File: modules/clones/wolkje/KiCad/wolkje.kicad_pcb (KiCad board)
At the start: 2 copper layers, 90 x 110 mm, 137 parts, among them J1 IN_L, J10 SIZE_IN, J11 BLEND_IN, J12 TEXTURE_IN, J2 OUT_L, J3 IN_R, J4 OUT_R, J5 FREEZE_IN, J6 V/OCT_IN, J7 POSITION_IN, J8 TRIGGER_IN, J9 DENSITY_IN, Q1 MMBT3904, Q2 MMBT3904, SW1 SW_ML6, SW2 SW_ML6, SW3 SW_RESEVERD, SW4 SW_MODE, U1 TL072, U2 TL072, U4 AMS1117-3.3, U5 LM4040DBZ-10, U6 AMS1117-3.3, U7 MCP6002, U8 MCP6004, U9 74HC595

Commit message: Update readme, get ready for third PCB run
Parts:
- removed the G*** at (83.0, 96.5)
- removed the G*** at (124.0, 65.0)
- removed the G*** at (119.0, 65.0)
- removed the G*** at (82.4, 88.9)
- removed REF**: WEEE-Logo_5.6x8mm_SilkScreen, Symbol:WEEE-Logo_5.6x8mm_SilkScreen
- added G***: LOGO, Synth:lenimal_logo_full, F.Cu at (95.0, 127.0)
- added G***: LOGO, synth-gfx:wolkje, F.Cu at (95.0, 97.5)
- added G***: LOGO, synth-gfx:wolkje, B.Cu at (70.5, 72.2)
- added G***: LOGO, Synth:lenimal_logo_full, B.Cu at (95.0, 62.5)
- C14, C9: footprint Capacitor_THT:CP_Radial_D6.3mm_P2.50mm -> Capacitor_THT:CP_Radial_D5.0mm_P2.50mm
- D5: value LED_2 -> LED_4
- D6: value LED_1 -> LED_3
- D7: value LED_4 -> LED_2
- D8: value LED_3 -> LED_1
- R38: value 680R -> 2K
- R46, R47, R48, R49, R50, R51, R52, R53: moved to F.Cu
- U4: value AMS1117-3.3 -> LM1117-3.3; footprint Package_TO_SOT_SMD:SOT-223-3_TabPin2 -> Package_TO_SOT_SMD:TO-252-3_TabPin2
- U5: footprint Package_TO_SOT_THT:TO-92_Inline -> Package_TO_SOT_SMD:SOT-23
- U6: value AMS1117-3.3 -> LM1117-3.3
- moved R17 85.2 mm to (52.5, 71.8), turned to 0 degrees
- moved D1 84.1 mm to (53.0, 74.0)
- moved C9 82.8 mm to (53.2, 69.0)
- moved H1 79.1 mm to (54.2, 91.0)
- moved D3 76.1 mm to (61.8, 94.2), turned to -90 degrees
- moved C11 75.6 mm to (67.4, 100.8), turned to 0 degrees
- moved U5 74.9 mm to (67.3, 97.8)
- moved R19 74.7 mm to (67.2, 95.0), turned to 0 degrees
- moved R20 74.7 mm to (64.2, 93.8), turned to -90 degrees
- moved C10 74.2 mm to (58.5, 68.8), turned to 90 degrees
- moved C14 72.8 mm to (53.2, 103.5)
- moved TP4 72.0 mm to (59.0, 72.8), turned to -90 degrees
- moved TP3 69.7 mm to (71.0, 100.8)
- moved C15 69.2 mm to (58.4, 103.2), turned to 90 degrees
- moved TP1 65.1 mm to (62.0, 85.9), turned to -90 degrees
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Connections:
- C27 pad 2: Net-(U8C--) -> Net-(U8A--)
- C28 pad 2: Net-(U8A--) -> Net-(U8B--)
- C29 pad 2: Net-(U8B--) -> Net-(U8C--)
- R33 pad 2: Net-(U8C--) -> Net-(U8A--)
- R35 pad 1: Net-(U8C--) -> Net-(U8A--)
- R37 pad 2: Net-(U8C--) -> Net-(U8A--)
- R39 pad 2: Net-(U8A--) -> Net-(U8B--)
- R41 pad 1: Net-(U8A--) -> Net-(U8B--)
- R42 pad 2: Net-(U8A--) -> Net-(U8B--)
- R43 pad 2: Net-(U8B--) -> Net-(U8C--)
- R44 pad 1: Net-(U8B--) -> Net-(U8C--)
- R45 pad 2: Net-(U8B--) -> Net-(U8C--)
- U1 pad 4: +12V -> -12V
- U1 pad 8: -12V -> +12V
- U2 pad 4: +12V -> -12V
- U2 pad 8: -12V -> +12V
- U8 pad 1: /inputs/BLEND_CV -> /inputs/SIZE_CV
- U8 pad 7: /inputs/TEXTURE_CV -> /inputs/BLEND_CV
- U8 pad 8: /inputs/SIZE_CV -> /inputs/TEXTURE_CV
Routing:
- net /inputs/FREEZE_LED: track 2.79 -> 132.0 mm
- net -10V: track 210.2 -> 91.9 mm, vias 6 -> 1
- net Net-(R38-Pad1): track 112.3 -> 6.13 mm, vias 1 -> 0
- net Net-(Q1-B): track 71.0 -> 172.8 mm, vias 2 -> 0
- net Net-(Q2-B): track 56.5 -> 150.5 mm
- net GNDREF: track 88.8 -> 0.00 mm, vias 24 -> 56
- net -12V: track 246.1 -> 177.6 mm, vias 0 -> 2
- net /inputs/TEXTURE: track 95.1 -> 38.5 mm, vias 1 -> 0
- net +12V: track 350.3 -> 295.1 mm, vias 1 -> 2
- net /inputs/BLEND: track 110.4 -> 61.3 mm, vias 1 -> 3
- net +3.3VA: track 186.1 -> 150.3 mm, vias 0 -> 1
- net Net-(U8C--): track 35.0 -> 70.0 mm, vias 2 -> 0
- net Net-(D7-A2): track 40.8 -> 6.51 mm
- net /inputs/PITCH: track 72.2 -> 38.4 mm, vias 0 -> 2
- net +3.3V: track 97.9 -> 128.8 mm, vias 2 -> 3
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- added copper zone on B.Cu, net GNDREF
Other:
- board text added: "+12V"
- board text added: "+3.3V"
- board text added: "+3.3VA"
- board text added: "-10V"
- board text added: "-12V"
- board text added: "GND"
- board text added: "LENIMAL PCB DESIGN 01.2025"
- board text added: "Wolkje / Weathering (The Storm)"
- board text added: "board-v2"
- board text added: "cc-by-sa - Emilie Gillet [Mutable Instruments]"
- board text removed: "Based on the designs by MI, THX Emilie Gillet"
- board text removed: "LENIMAL PCB DESIGN 11.24"
- board text removed: "WOLKJE"
- board text removed: "rev.1"

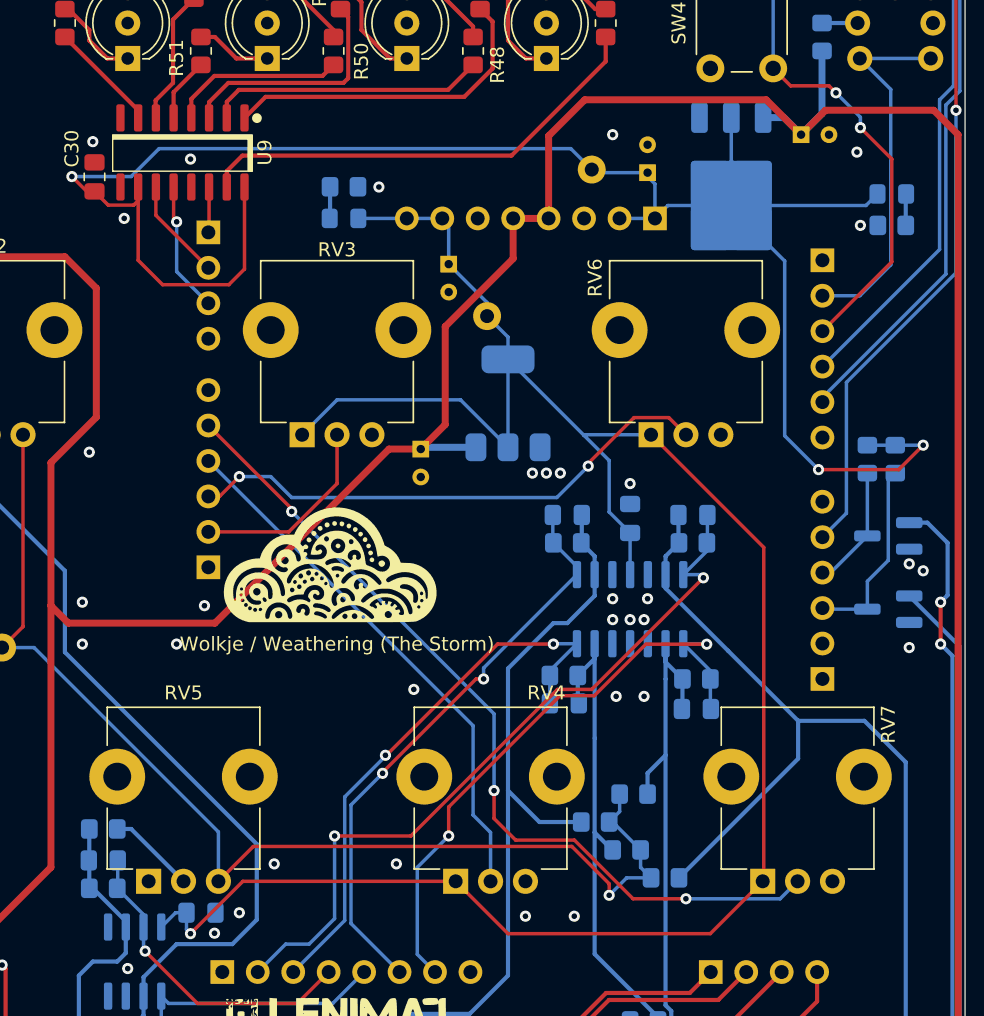
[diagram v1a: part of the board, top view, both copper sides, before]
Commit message: Preperation for Run3, wolkje, ricochet readme and final exports
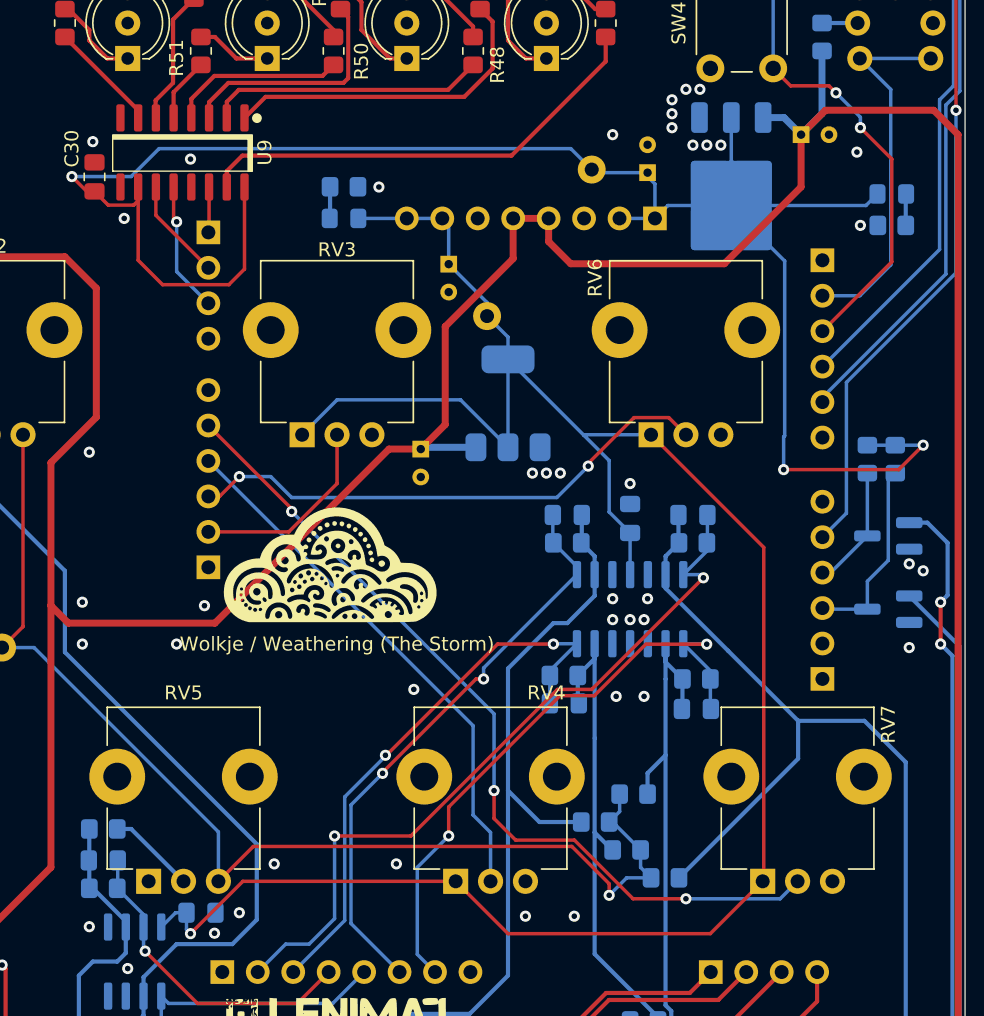
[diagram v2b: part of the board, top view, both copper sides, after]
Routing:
- net +3.3V: track 128.8 -> 130.4 mm
- net GNDREF: vias 56 -> 65

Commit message: finished clouds clone (weathering/the storm)
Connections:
- RV1 pad 1: Net-(R2-Pad2) -> Net-(R8-Pad1)
- RV1 pad 2: Net-(R11-Pad1) -> Net-(R8-Pad1)
- RV1 pad 3: Net-(R11-Pad1) -> Net-(R1-Pad2)
- RV1 pad 4: Net-(R1-Pad2) -> Net-(R11-Pad1)
- RV1 pad 5: Net-(R8-Pad1) -> Net-(R11-Pad1)
- RV1 pad 6: Net-(R8-Pad1) -> Net-(R2-Pad2)
- RV2 pad 1: GNDREF -> -10V
- RV2 pad 3: -10V -> GNDREF
- RV3 pad 1: +3.3VA -> GNDREF
- RV3 pad 3: GNDREF -> +3.3VA
- RV4 pad 1: +3.3VA -> GNDREF
- RV4 pad 3: GNDREF -> +3.3VA
- RV5 pad 1: GNDREF -> -10V
- RV5 pad 3: -10V -> GNDREF
- RV6 pad 1: +3.3VA -> GNDREF
- RV6 pad 3: GNDREF -> +3.3VA
- RV7 pad 1: +3.3VA -> GNDREF
- RV7 pad 3: GNDREF -> +3.3VA
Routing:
- net +3.3VA: track 150.3 -> 163.4 mm, vias 1 -> 2
- net Net-(R2-Pad2): track 15.6 -> 5.74 mm
- net Net-(R1-Pad2): track 11.9 -> 21.5 mm, vias 0 -> 1
- net Net-(R32-Pad1): track 6.30 -> 14.8 mm, vias 0 -> 1
- net -10V: track 91.9 -> 98.4 mm
- net Net-(R8-Pad1): track 16.0 -> 18.9 mm
- net Net-(R11-Pad1): track 14.7 -> 13.1 mm, vias 0 -> 1
- net /inputs/PITCH: track 38.4 -> 37.7 mm
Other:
- board text added: "board-v3"
- board text removed: "board-v2"
